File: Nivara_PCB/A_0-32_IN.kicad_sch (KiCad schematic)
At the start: 5 parts

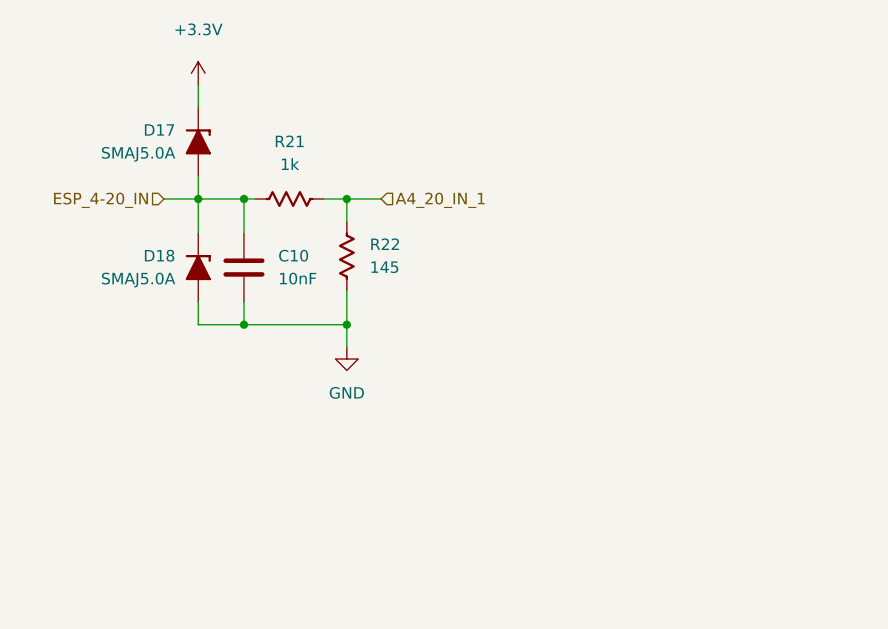
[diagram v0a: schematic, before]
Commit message: Cambios realizados en el PCB y el esquema de Nivara_PCB.
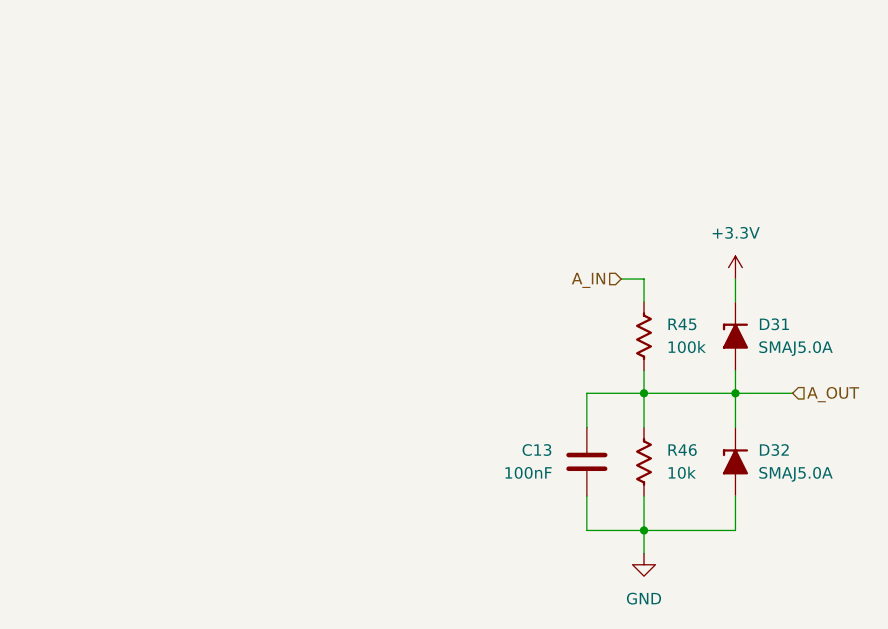
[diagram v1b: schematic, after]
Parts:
- removed C10: 10nF, PCM_Capacitor_SMD_AKL:C_0603_1608Metric, symbol PCM_Capacitor_US_AKL:C_0603
- removed D17, D18: SMAJ5.0A, PCM_Diode_SMD_AKL:D_SMA, symbol PCM_Diode_TVS_AKL:SMAJ5.0A
- removed R21: 1k, PCM_Resistor_SMD_AKL:R_0603_1608Metric, symbol PCM_Resistor_US_AKL:R_0603
- removed R22: 145, PCM_Resistor_SMD_AKL:R_0805_2012Metric, symbol PCM_Resistor_US_AKL:R_0805
- added C13: 100nF, PCM_Capacitor_SMD_AKL:C_0603_1608Metric, symbol PCM_Capacitor_US_AKL:C_0603
- added D31, D32: SMAJ5.0A, PCM_Diode_SMD_AKL:D_SMA, symbol PCM_Diode_TVS_AKL:SMAJ5.0A
- added R45: 100k, PCM_Resistor_SMD_AKL:R_0603_1608Metric, symbol PCM_Resistor_US_AKL:R_0603
- added R46: 10k, PCM_Resistor_SMD_AKL:R_0603_1608Metric, symbol PCM_Resistor_US_AKL:R_0603
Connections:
- net +3.3V: now also D31.1 (K)
- net GND: now also C13.2, D32.2 (A), R46.1
- new net A_IN: R45.2
- new net A_OUT: C13.1, D31.2 (A), D32.1 (K), R45.1, R46.2

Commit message: Cambios realizados en los archivos de Nivara_PCB.
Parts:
- C13: symbol PCM_Capacitor_US_AKL:C_0603 -> EasyEDA:C_0603
- D31, D32: symbol PCM_Diode_TVS_AKL:SMAJ5.0A -> EasyEDA:SMAJ5.0A
- R45, R46: symbol PCM_Resistor_US_AKL:R_0603 -> EasyEDA:R_0603
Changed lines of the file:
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@@
 	)
 	(symbol
-		(lib_id "power:GND")
+		(lib_id "EasyEDA:GND")
 		(at 105.41 99.06 0)
 		(unit 1)
@@
 	)
 	(symbol
-		(lib_id "PCM_Diode_TVS_AKL:SMAJ5.0A")
+		(lib_id "EasyEDA:SMAJ5.0A")
 		(at 115.57 74.93 90)
 		(unit 1)
@@
 	)
 	(symbol
-		(lib_id "power:+3.3V")
+		(lib_id "EasyEDA:+3.3V")
 		(at 115.57 68.58 0)
 		(unit 1)
@@
 	)
 	(symbol
-		(lib_id "PCM_Resistor_US_AKL:R_0603")
+		(lib_id "EasyEDA:R_0603")
 		(at 105.41 74.93 180)
 		(unit 1)
@@
 	)
 	(symbol
-		(lib_id "PCM_Diode_TVS_AKL:SMAJ5.0A")
+		(lib_id "EasyEDA:SMAJ5.0A")
 		(at 115.57 88.9 90)
 		(unit 1)
@@
 	)
 	(symbol
-		(lib_id "PCM_Resistor_US_AKL:R_0603")
+		(lib_id "EasyEDA:R_0603")
 		(at 105.41 88.9 180)
 		(unit 1)
@@
 	)
 	(symbol
-		(lib_id "PCM_Capacitor_US_AKL:C_0603")
+		(lib_id "EasyEDA:C_0603")
 		(at 99.06 88.9 0)
 		(mirror y)
